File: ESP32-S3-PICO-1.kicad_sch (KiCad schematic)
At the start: 20 parts, among them U401 ESP32-S3-PICO-1-N8R2

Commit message: Update CAN_Interface.kicad_sch, ESP32-S3 D1 Pico Board.kicad_sch, ESP32-S3 Pico D1.kicad_pcb, and 5 more files
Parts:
- gave numbers to parts that had none: 3
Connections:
- net IO21: now also R406.2; no longer U401.27 (GPIO21)
- net IO39: now also U401.44 (MTCK/GPIO39); no longer R406.1
- net EN renamed EN/~{RST}
- new net GPIO21: R406.1, U401.27 (GPIO21)
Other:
- moved on the sheet: R406
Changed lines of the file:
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@@
 	(wire
 		(pts
-			(xy 161.29 81.28) (xy 157.48 81.28)
+			(xy 157.48 81.28) (xy 170.18 81.28)
 		)
 		(stroke
@@
 	(wire
 		(pts
-			(xy 101.6 127) (xy 116.84 127)
+			(xy 101.6 127) (xy 105.41 127)
 		)
 		(stroke
@@
 	(wire
 		(pts
-			(xy 170.18 81.28) (xy 168.91 81.28)
+			(xy 170.18 73.66) (xy 157.48 73.66)
 		)
 		(stroke
@@
 	(wire
 		(pts
-			(xy 170.18 73.66) (xy 157.48 73.66)
+			(xy 167.64 99.06) (xy 170.18 99.06)
 		)
 		(stroke
@@
 	(wire
 		(pts
-			(xy 167.64 99.06) (xy 170.18 99.06)
+			(xy 104.14 53.34) (xy 109.22 53.34)
 		)
 		(stroke
@@
 	(wire
 		(pts
-			(xy 104.14 53.34) (xy 109.22 53.34)
+			(xy 113.03 106.68) (xy 116.84 106.68)
 		)
 		(stroke
@@
 	(wire
 		(pts
-			(xy 113.03 106.68) (xy 116.84 106.68)
+			(xy 109.22 53.34) (xy 114.3 53.34)
 		)
 		(stroke
@@
 	(wire
 		(pts
-			(xy 109.22 53.34) (xy 114.3 53.34)
+			(xy 152.4 137.16) (xy 154.94 137.16)
 		)
 		(stroke
@@
 	(wire
 		(pts
-			(xy 152.4 137.16) (xy 154.94 137.16)
+			(xy 113.03 127) (xy 116.84 127)
 		)
 		(stroke
@@
 		)
 	)
+	(label "GPIO21"
+		(at 114.3 127 0)
+		(effects
+			(font
+				(size 0.635 0.635)
+			)
+			(justify bottom)
+		)
+	)
 	(label "GPIO12"
 		(at 114.3 104.14 0)
@@
 		)
 	)
-	(hierarchical_label "EN"
+	(hierarchical_label "EN{slash}~{RST}"
 		(shape input)
 		(at 170.18 73.66 0)
@@
 	(symbol
 		(lib_id "Device:R")
-		(at 165.1 81.28 270)
+		(at 109.22 127 270)
 		(unit 1)
 		(exclude_from_sim no)
@@
 		(on_board yes)
 		(dnp no)
-		(property "Reference" "R?"
-			(at 161.29 80.645 90)
+		(property "Reference" "R406"
+			(at 105.41 126.365 90)
 			(effects
 				(font
@@
 		)
 		(property "Value" "33R"
-			(at 165.1 81.28 90)
+			(at 109.22 127 90)
 			(effects
 				(font
@@
 		)
 		(property "Footprint" "My Resistors:R_0201_Dense"
-			(at 165.1 79.502 90)
+			(at 109.22 125.222 90)
 			(effects
 				(font
@@
 		)
 		(property "Datasheet" "https://yageogroup.com/content/datasheet/asset/file/PYU-AC_51_ROHS_L"
-			(at 165.1 81.28 0)
+			(at 109.22 127 0)
 			(effects
 				(font
@@
 		)
 		(property "Description" "RES SMD 33 OHM 1% 1/20W 0201 AEC-Q200"
-			(at 165.1 81.28 0)
+			(at 109.22 127 0)
 			(effects
 				(font
@@
 		)
 		(property "Manufacturer" "YAGEO"
-			(at 165.1 81.28 90)
+			(at 109.22 127 90)
 			(effects
 				(font
@@
 		)
 		(property "Manufacturer Part Number" "AC0201FR-0733RL"
-			(at 165.1 81.28 90)
+			(at 109.22 127 90)
 			(effects
 				(font
@@
 		)
 		(property "LCSC" "C226514"
-			(at 165.1 81.28 90)
+			(at 109.22 127 90)
 			(effects
 				(font
@@
 		)
 		(property "Distributor Link 1" "https://www.digikey.com/en/products/detail/yageo/AC0201FR-0733RL/5894558"
-			(at 165.1 81.28 90)
+			(at 109.22 127 90)
 			(effects
 				(font
@@
 		)
 		(property "Distributor Link 2" "https://www.mouser.com/ProductDetail/YAGEO/AC0201FR-0733RL?qs=NgbZBzc1CyGsdL%2FSauAQCA%3D%3D"
-			(at 165.1 81.28 90)
+			(at 109.22 127 90)
 			(effects
 				(font
@@
 			(project "ESP32-S3 Pico D1"
 				(path "/67f7b1e1-e87f-421a-8424-bb26889ab157/2e11fda6-397f-44e4-8131-fa876b821c34/3412d0f1-7c6a-4bf4-a082-dea1354cc758"
-					(reference "R?")
+					(reference "R406")
 					(unit 1)
 				)
@@
 		(on_board yes)
 		(dnp no)
-		(property "Reference" "R?"
+		(property "Reference" "R407"
 			(at 171.45 100.965 90)
 			(effects
@@
 			(project "ESP32-S3 Pico D1"
 				(path "/67f7b1e1-e87f-421a-8424-bb26889ab157/2e11fda6-397f-44e4-8131-fa876b821c34/3412d0f1-7c6a-4bf4-a082-dea1354cc758"
-					(reference "R?")
+					(reference "R407")
 					(unit 1)
 				)
@@
 		(on_board yes)
 		(dnp no)
-		(property "Reference" "R?"
+		(property "Reference" "R408"
 			(at 171.45 103.505 90)
 			(effects
@@
 			(project "ESP32-S3 Pico D1"
 				(path "/67f7b1e1-e87f-421a-8424-bb26889ab157/2e11fda6-397f-44e4-8131-fa876b821c34/3412d0f1-7c6a-4bf4-a082-dea1354cc758"
-					(reference "R?")
+					(reference "R408")
 					(unit 1)
 				)

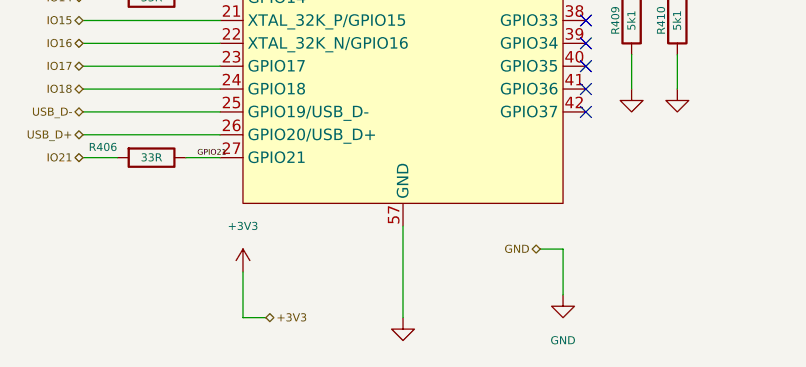
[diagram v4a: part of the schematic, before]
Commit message: fixed hierarchical sheets; replaced pin headers with ESP32-S3_D1_Pico symbol
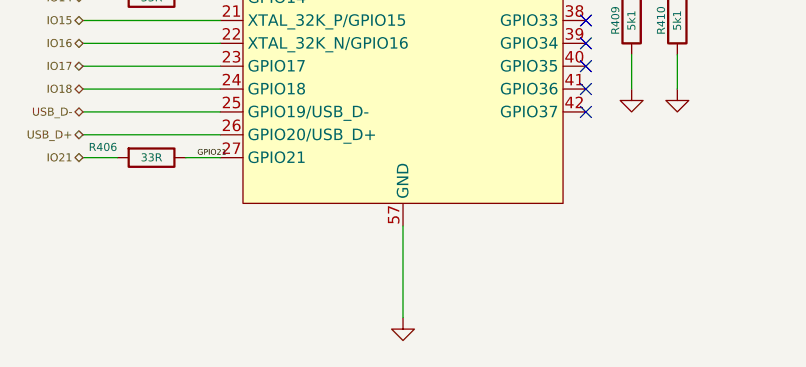
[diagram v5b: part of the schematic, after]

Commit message: Update ESP32-S3 Pico D1-Main.kicad_sch, ESP32-S3 Pico D1.kicad_pcb, ESP32-S3 Pico D1.kicad_prl, and 7 more files
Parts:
- added +V401, +V402: +3V3, symbol My Power Management:+V (Local)
- added GND401, GND402, GND403, GND404, GND405, GND406, GND407, GND408: GND, symbol My Power Management:GND (Local)
- R401, R402, R403, R404, R405, R406, R407, R408, R409, R410: footprint My Resistors:R_0201_Dense -> My Resistors:R_0201_Nominal
- R411: Distributor Link 1 https://www.digikey.com/en/products/detail/yageo/AC0201JR-1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 -> (none); Distributor Link 2 https://www.mouser.com/ProductDetail/YAGEO/AC0201JR-130RL?q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 -> https://www.mouser.com/ProductDetail/Royalohm/0201WMF0000TE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; LCSC C6491732 -> C473473; Manufacturer YAGEO -> UNI-ROYAL(Uniroyal Elec); Manufacturer Part Number AC0201JR-130RL -> 0201WMF0000TEE
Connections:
- net +3V3: now also +V401.1, +V402.1
- net GND: now also GND401.1 (GND), GND402.1 (GND), GND403.1 (GND), GND404.1 (GND), GND405.1 (GND), GND406.1 (GND), GND407.1 (GND), GND408.1 (GND)
